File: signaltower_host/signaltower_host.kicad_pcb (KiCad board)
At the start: 2 copper layers, 71.5 x 60 mm, 12 parts, among them J1 uUSBconecter_ZX62R-B-5P, J2 GB-TB-50LBS-2P, J3 5051100892_FFC-FPCconecter, J4 PSS-720102-05, U1 BD50C0AWFP, U2 RK7002BMT-116, U3 Lazurite_920J

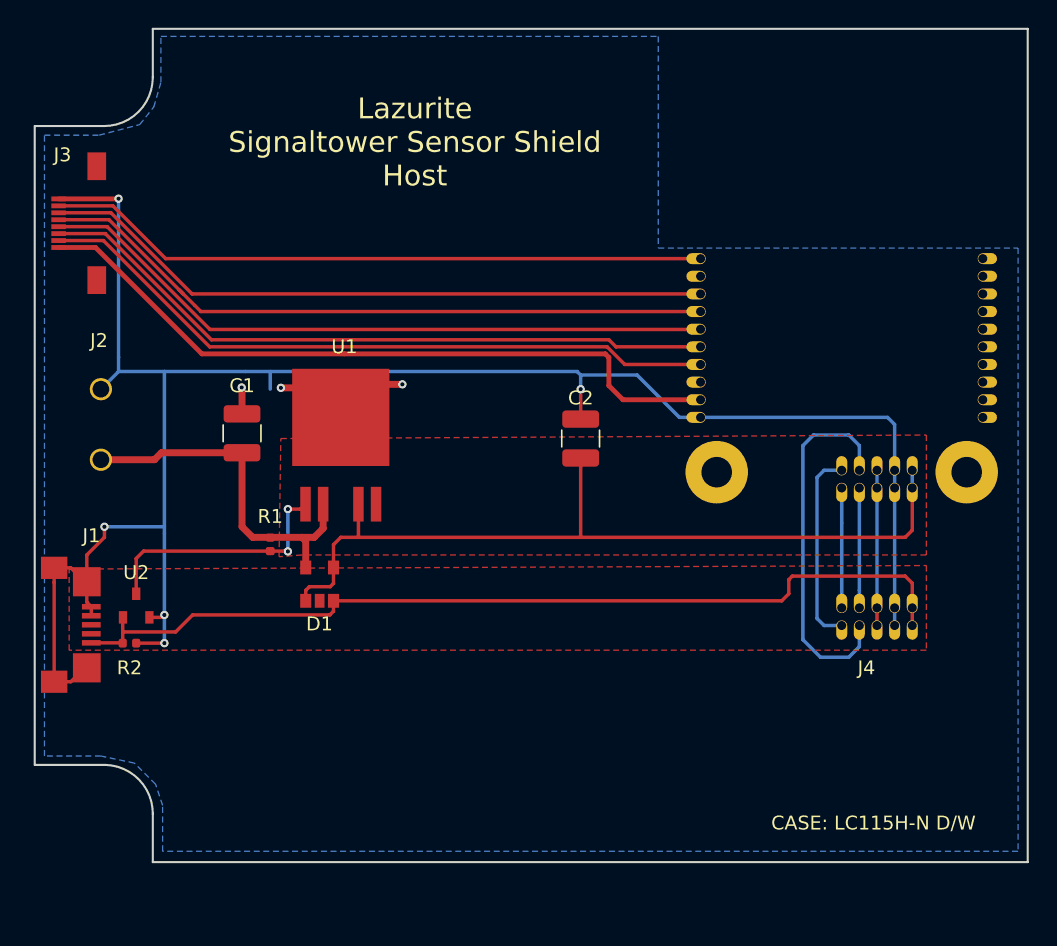
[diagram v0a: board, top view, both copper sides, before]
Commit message: update signal sensor host/slave
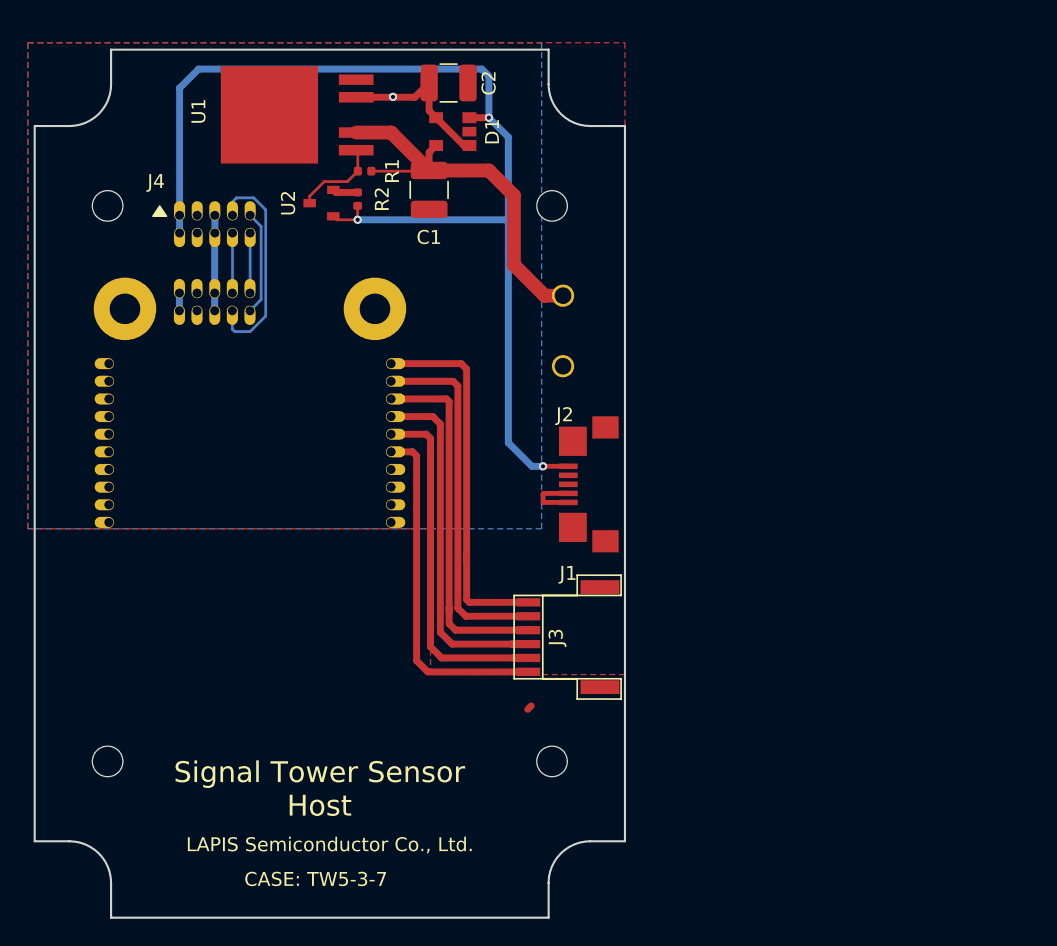
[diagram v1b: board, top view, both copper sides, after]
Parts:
- added H1: MountingHole, MountingHole:MountingHole_2.2mm_M2, F.Cu at (96.8, 62.8)
- added H2: MountingHole, MountingHole:MountingHole_2.2mm_M2, F.Cu at (96.8, 102.8)
- added H3: MountingHole, MountingHole:MountingHole_2.2mm_M2, F.Cu at (128.8, 62.8)
- added H4: MountingHole, MountingHole:MountingHole_2.2mm_M2, F.Cu at (128.8, 102.8)
- J3: value 5051100892_FFC-FPCconecter -> Conn_01x06_Female; footprint lazurite_footprint:FFC-FPC_5051100892 -> Connector_JST:JST_NSH_SM06B_1mm_Horizonal
- moved J4 56.1 mm to (104.5, 63.4), turned to 0 degrees
- moved U3 46.6 mm to (107.0, 85.5), turned to 0 degrees
- moved J3 44.7 mm to (127.0, 93.8)
- moved J1 41.0 mm to (132.6, 82.8), turned to 90 degrees
- moved R2 35.9 mm to (114.8, 62.3), turned to 90 degrees
- moved D1 35.5 mm to (122.8, 57.4), turned to 90 degrees
- moved J2 33.9 mm to (129.5, 71.8), turned to 270 degrees
- moved U2 33.0 mm to (113.0, 62.5), turned to 90 degrees
- moved U1 28.1 mm to (114.7, 56.2), turned to 90 degrees
- moved R1 27.7 mm to (115.2, 60.2), turned to 180 degrees
- moved C2 27.3 mm to (121.3, 53.9), turned to 0 degrees
- moved C1 22.1 mm to (119.9, 61.6), turned to 270 degrees
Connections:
- J1 pad 2: (no net) -> Net-(J1-Pad2)
- J1 pad 3: (no net) -> Net-(J1-Pad3)
- U1 pad 5: (no net) -> Net-(U1-Pad5)
- U3 pad 10: (no net) -> Net-(U3-Pad10)
- U3 pad 11: (no net) -> Net-(U3-Pad11)
- U3 pad 12: (no net) -> Net-(U3-Pad12)
- U3 pad 13: (no net) -> Net-(U3-Pad13)
- U3 pad 14: (no net) -> Net-(J3-Pad4)
- U3 pad 15: Net-(J3-Pad2) -> Net-(J3-Pad3)
- U3 pad 16: Net-(J3-Pad3) -> Net-(J3-Pad2)
- U3 pad 17: Net-(J3-Pad4) -> Net-(J3-Pad1)
- U3 pad 18: Net-(J3-Pad5) -> Net-(U3-Pad18)
- U3 pad 19: Net-(J3-Pad6) -> Net-(U3-Pad19)
- U3 pad 2: Net-(J3-Pad7) -> Net-(U3-Pad2)
- U3 pad 28: Net-(J3-Pad1) -> Net-(J3-Pad5)
- U3 pad 29: GND -> Net-(J3-Pad6)
- U3 pad 3: (no net) -> Net-(U3-Pad3)
- U3 pad 4: (no net) -> Net-(U3-Pad4)
- U3 pad 5: (no net) -> Net-(U3-Pad5)
- U3 pad 6: (no net) -> Net-(U3-Pad6)
- U3 pad 7: (no net) -> Net-(U3-Pad7)
- U3 pad 8: (no net) -> Net-(U3-Pad8)
- U3 pad 9: (no net) -> Net-(U3-Pad9)
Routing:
- net GND: track 155.3 -> 6.10 mm, vias 8 -> 0
- net Net-(J3-Pad7): track 47.8 -> 0.00 mm
- net +5V: track 60.6 -> 13.0 mm, vias 0 -> 1
- net Net-(J3-Pad1): track 52.7 -> 25.6 mm
- net Net-(J3-Pad5): track 49.4 -> 26.3 mm
- net Net-(J3-Pad2): track 49.9 -> 26.9 mm
- net Net-(J3-Pad3): track 49.6 -> 26.7 mm
- net Net-(J3-Pad4): track 49.3 -> 26.5 mm
- net Net-(J3-Pad6): track 48.6 -> 27.1 mm
- net +5VP: track 66.9 -> 80.8 mm, vias 0 -> 3
- net Net-(R1-Pad2): track 18.3 -> 6.27 mm, vias 2 -> 0
- net /TEST0: track 27.3 -> 15.7 mm
- net /0: track 14.1 -> 7.53 mm
- net /TEST1N: track 8.64 -> 4.33 mm
- net +3V3: track 11.2 -> 6.87 mm
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- added copper zone on B.Cu, net +5V
- added copper zone on F.Cu, net GND
- removed copper zone on F.Cu, net +5V
- removed copper zone on F.Cu, net +5VP
- removed copper zone on B.Cu, net GND
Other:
- board size 71.5 x 60 mm -> 42.5 x 62.5 mm
- board text added: "CASE: TW5-3-7"
- board text added: "LAPIS Semiconductor Co., Ltd."
- board text added: "Signal Tower Sensor Host"
- board text removed: "CASE: LC115H-N D/W"
- board text removed: "Lazurite Signaltower Sensor Shield Host"

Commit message: signal_sensor-host signal_sensor-slave   サイズを小型化   コネクタを変更
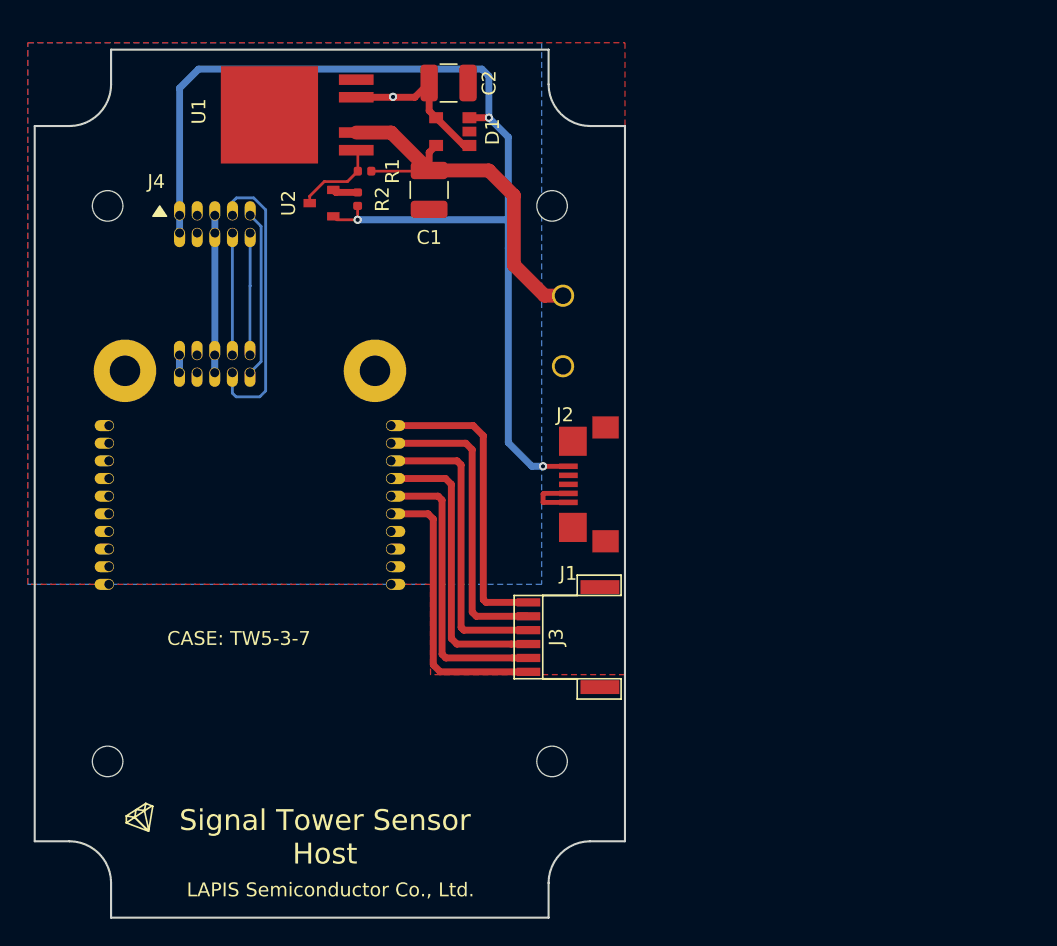
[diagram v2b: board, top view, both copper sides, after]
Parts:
- added REF**: Lazurite_logo, lazurite_footprint:Lazurite_logo, F.Cu at (99.4, 107.0)
- moved U3 4.46 mm to (107.0, 90.0)
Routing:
- net Net-(J3-Pad2): track 26.9 -> 21.2 mm
- net Net-(J3-Pad3): track 26.7 -> 21.3 mm
- net /TEST0: track 15.7 -> 21.0 mm
- net Net-(J3-Pad6): track 27.1 -> 22.1 mm
- net Net-(J3-Pad1): track 25.6 -> 20.8 mm
- net Net-(J3-Pad4): track 26.5 -> 21.8 mm
- net /0: track 7.53 -> 12.1 mm
- net +3V3: track 6.87 -> 11.4 mm
- net /TEST1N: track 4.33 -> 8.79 mm
- net /1: track 4.33 -> 8.79 mm
- net Net-(J3-Pad5): track 26.3 -> 21.9 mm

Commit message: signal tower sensor host/slave updated.
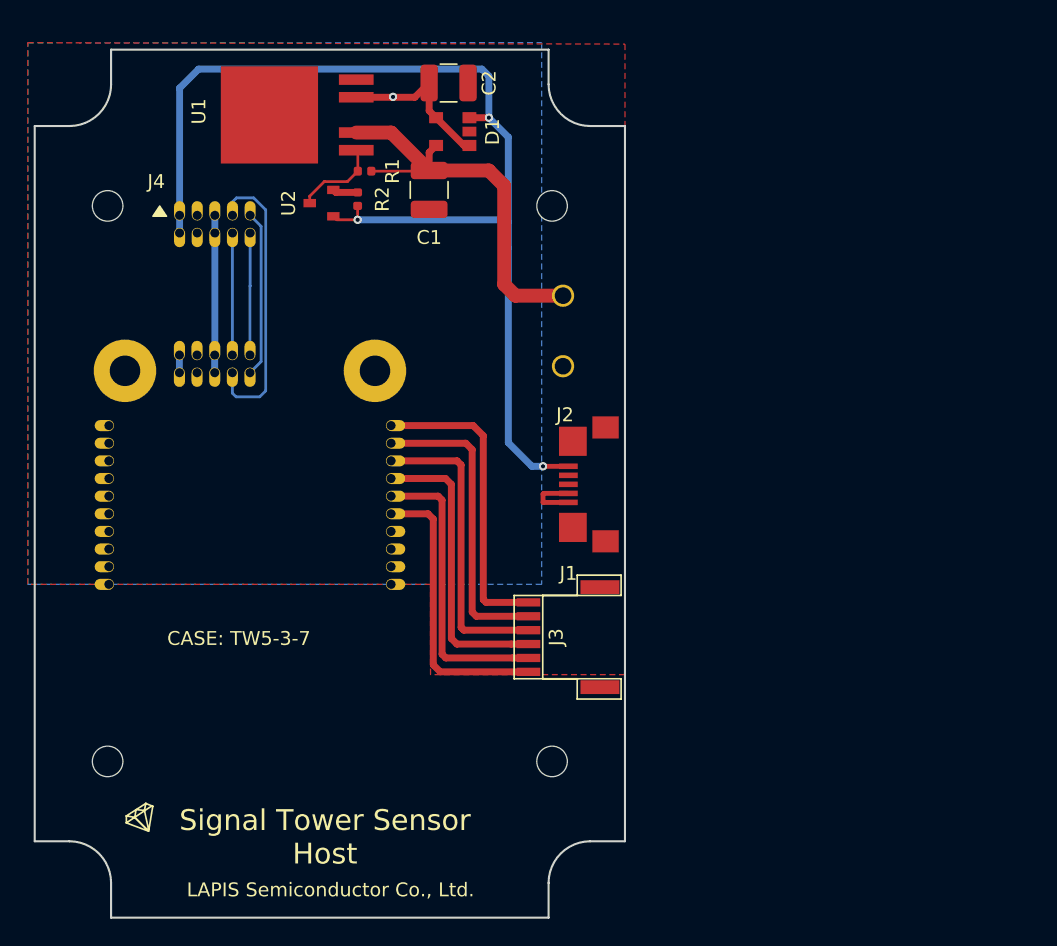
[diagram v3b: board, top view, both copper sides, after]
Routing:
- net +24V: track 28.9 -> 30.1 mm
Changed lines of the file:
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@@
       (drillshape 0)
       (scaleselection 1)
-      (outputdirectory "20200117_host/"))
+      (outputdirectory "20200722/"))
   )
   (net 0 "")
@@
   (segment (start 117.17 57.47) (end 114.65 57.47) (width 1) (layer F.Cu) (net 1))
   (segment (start 119.9 60.2) (end 117.17 57.47) (width 1) (layer F.Cu) (net 1))
-  (segment (start 129.54 69.215) (end 128.215 69.215) (width 1) (layer F.Cu) (net 1))
-  (segment (start 128.215 69.215) (end 126 67) (width 1) (layer F.Cu) (net 1))
-  (segment (start 126 67) (end 126 62) (width 1) (layer F.Cu) (net 1))
   (segment (start 124.2 60.2) (end 119.9 60.2) (width 1) (layer F.Cu) (net 1))
-  (segment (start 126 62) (end 124.2 60.2) (width 1) (layer F.Cu) (net 1))
   (segment (start 119.85 60.25) (end 119.9 60.2) (width 0.2) (layer F.Cu) (net 1))
   (segment (start 115.735 60.25) (end 119.85 60.25) (width 0.2) (layer F.Cu) (net 1))
   (segment (start 119.9 58.9) (end 120.4 58.4) (width 0.5) (layer F.Cu) (net 1))
   (segment (start 119.9 60.2) (end 119.9 58.9) (width 0.5) (layer F.Cu) (net 1))
+  (segment (start 129.54 69.215) (end 126.115 69.215) (width 1) (layer F.Cu) (net 1))
+  (segment (start 126.115 69.215) (end 125.3 68.4) (width 1) (layer F.Cu) (net 1))
+  (segment (start 125.3 61.3) (end 124.2 60.2) (width 1) (layer F.Cu) (net 1))
+  (segment (start 125.3 68.4) (end 125.3 61.3) (width 1) (layer F.Cu) (net 1))
   (segment (start 118.87 54.93) (end 119.9 53.9) (width 0.5) (layer F.Cu) (net 2))
   (segment (start 119.9 55.9) (end 120.4 56.4) (width 0.5) (layer F.Cu) (net 2))
@@
       (pts
         (xy 134 96.5) (xy 126.25 96.5) (xy 120 96.5) (xy 120 90) (xy 91 90)
-        (xy 91 51) (xy 134 51)
+        (xy 91 51) (xy 134 51.1)
       )
     )
+  )
+  (zone (net 0) (net_name "") (layer F.Cu) (hatch edge 0.508)
+    (connect_pads (clearance 0.508))
+    (min_thickness 0.254)
+    (keepout (tracks not_allowed) (vias not_allowed) (copperpour not_allowed))
+    (fill (arc_segments 32) (thermal_gap 0.508) (thermal_bridge_width 0.508))
+    (polygon
+      (pts
+        (xy 129.8 60.5) (xy 130.6 61.1) (xy 131.1 61.9) (xy 131.2 62.8) (xy 131 63.7)
+        (xy 130.7 64.3) (xy 129.9 64.9) (xy 129.1 65.2) (xy 128.7 65.2) (xy 127.9 65.1)
+        (xy 127.2 64.7) (xy 126.6 64) (xy 126.3 62.7) (xy 126.6 61.6) (xy 127.2 60.8)
+        (xy 128.7 60.3)
+      )
+    )
+  )
+  (zone (net 0) (net_name "") (layers F&B.Cu) (hatch edge 0.508)
+    (connect_pads (clearance 0.508))
+    (min_thickness 0.254)
+    (keepout (tracks not_allowed) (vias not_allowed) (copperpour not_allowed))
+    (fill (arc_segments 32) (thermal_gap 0.508) (thermal_bridge_width 0.508))
+    (polygon
+      (pts
+        (xy 98 60.6) (xy 98.8 61.4) (xy 99.2 62.4) (xy 99.1 63.4) (xy 98.7 64.2)
+        (xy 97.8 65) (xy 96.7 65.2) (xy 95.6 64.9) (xy 94.7 64.1) (xy 94.3 62.7)
+        (xy 94.6 61.4) (xy 95.4 60.7) (xy 96.7 60.3)
+      )
+    )
